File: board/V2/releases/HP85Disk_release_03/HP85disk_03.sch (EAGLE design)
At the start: 105 parts, among them J1 POWER_JACKSUPER_BOMB_DIGITY, J3 503398-1892, J4 USB_MINI-B_SMT, Q1 BSS138DW-7-F, U1 ATMEGA1284P-AUR, U10 MIC5205, U11 MAX811LEUS+T, U2 TPIC6A596DWRG4, U3 SN75ALS162DWR, U4 75ALS160, U6 SN74LVC1G32DCKR, U7 FT232RL, U8 TXS0104EDR, U9 LM1117, Y2 20MHz

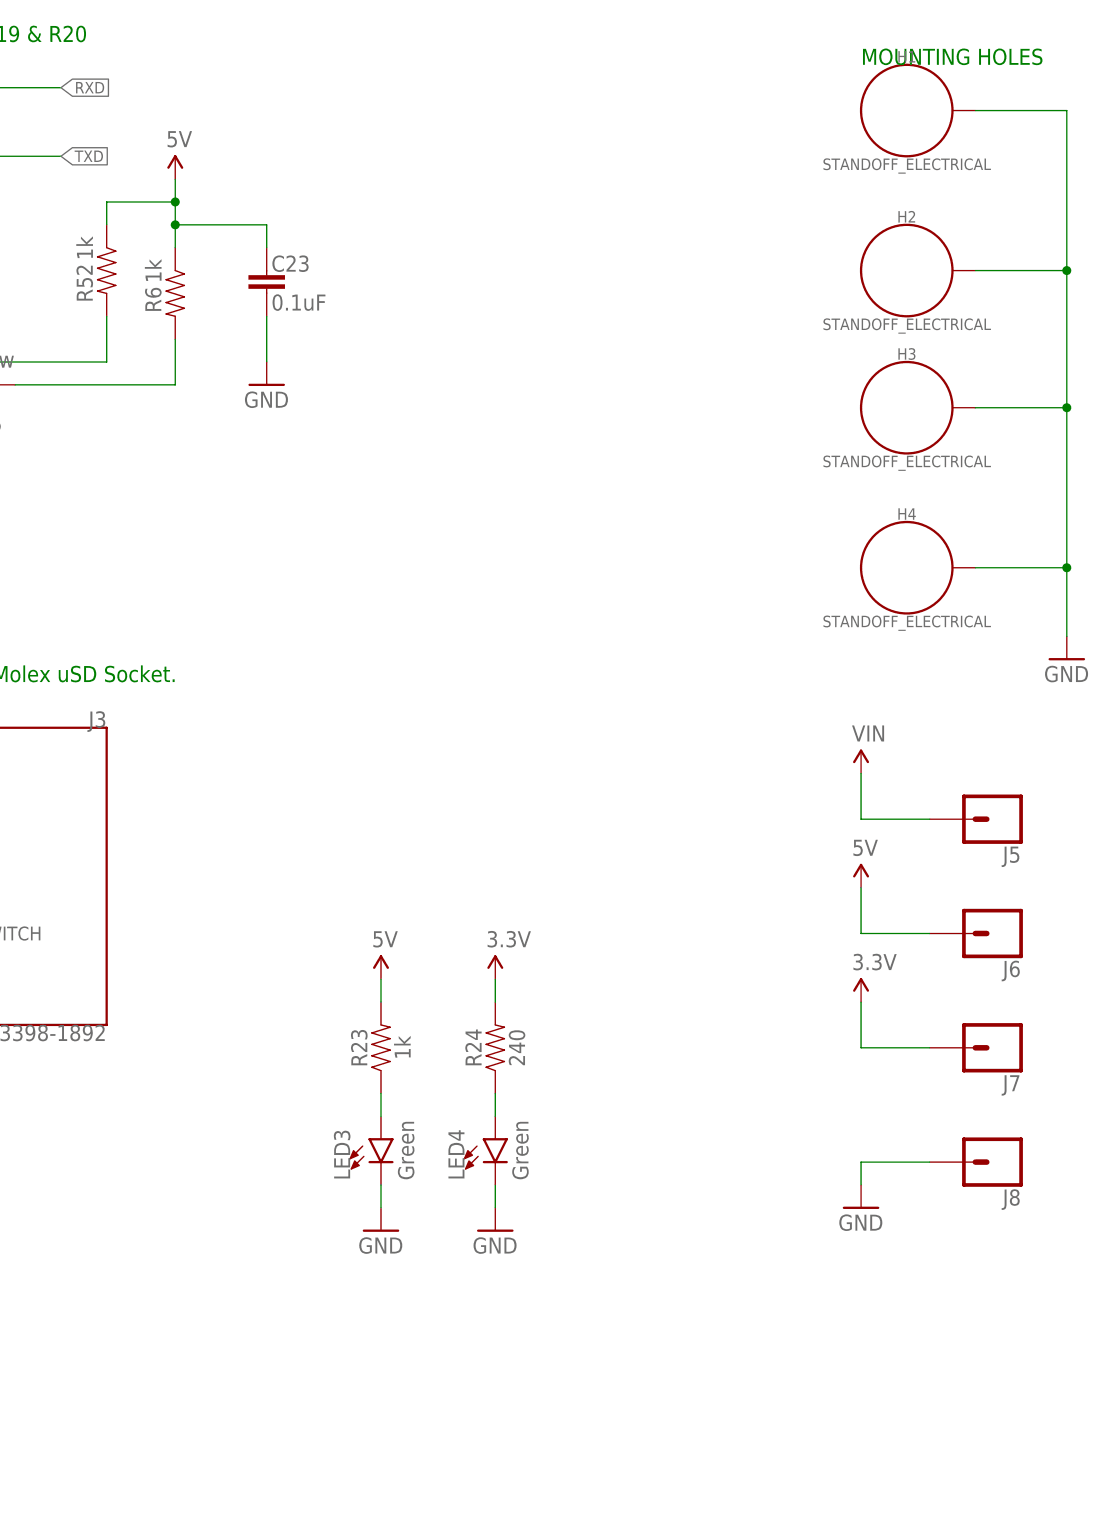
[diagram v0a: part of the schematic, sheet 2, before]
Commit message: Added RTC DS1703 - page 2 U5
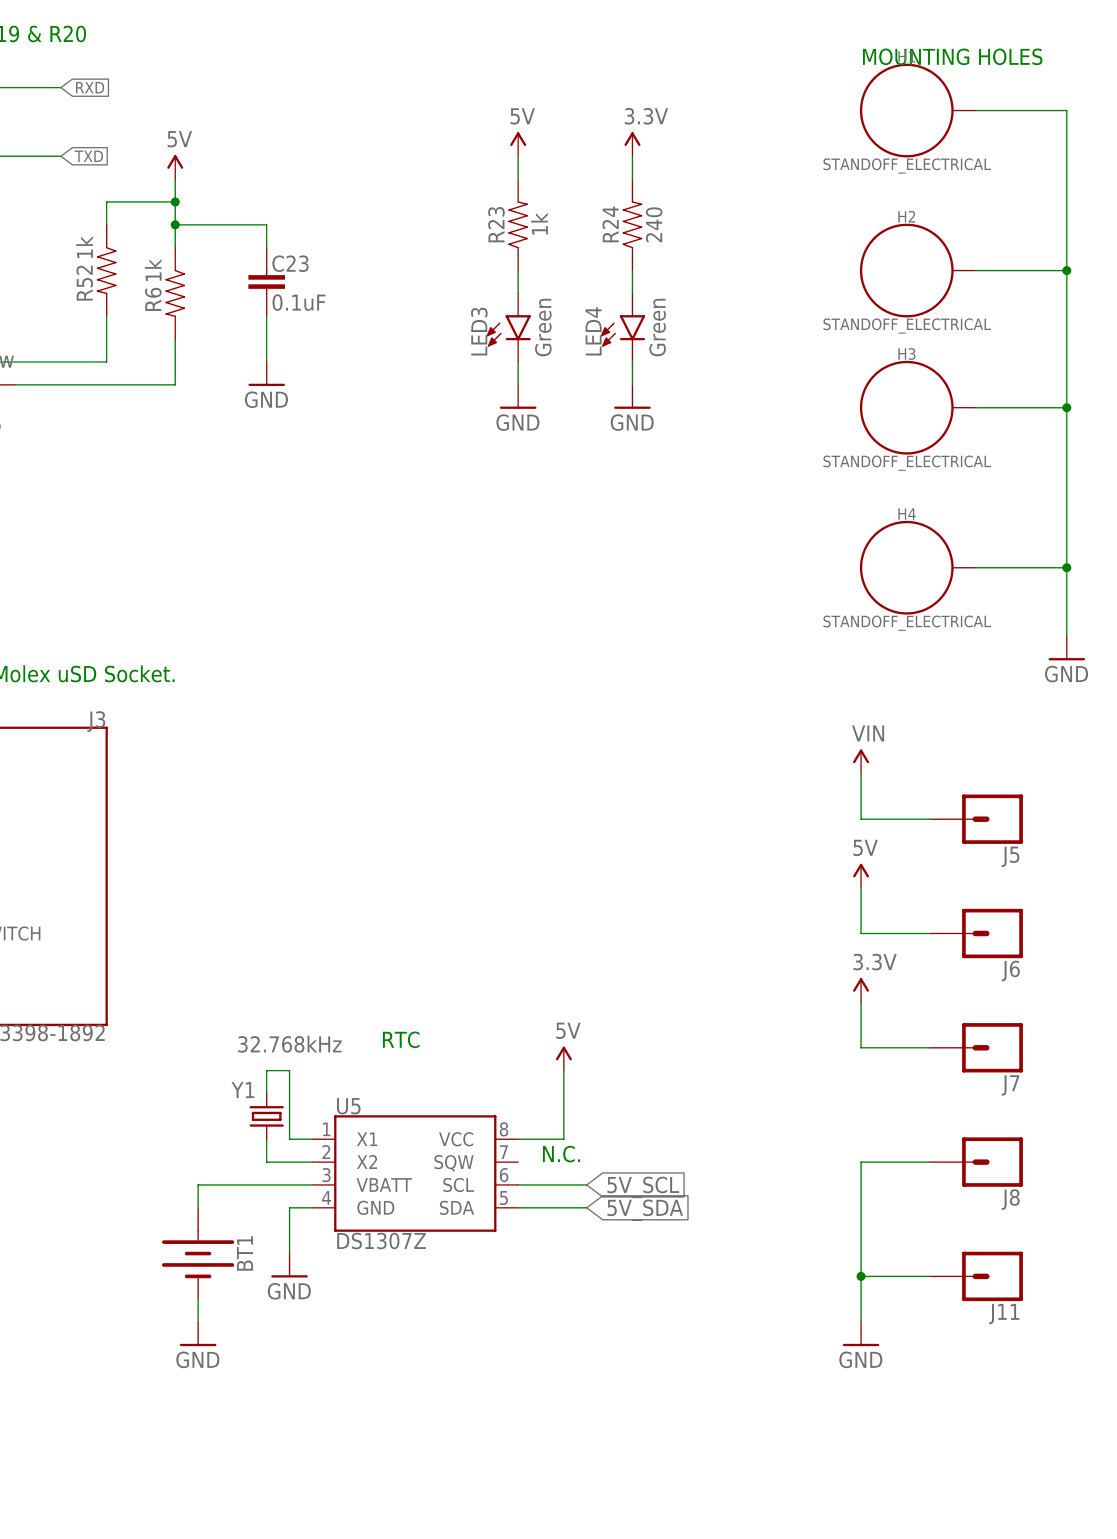
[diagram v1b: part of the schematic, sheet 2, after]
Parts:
- added BT1: (no value), SparkFun-Batteries:BATTERY-12MM_PTH
- added J11: (no value), SparkFun-Connectors:CONN_01
- added U5: DS1307Z, SparkFun-Clocks:DS1307Z
- added Y1: 32.768kHz, SparkFun-Clocks:CRYSTAL-32.768KHZSMD-2X6
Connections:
- new net N$16: U5.X1, Y1.2
- new net N$17: BT1.+, U5.VBATT
- new net N$18: U5.X2, Y1.1
- net 5V: now also U5.VCC
- net 5V_SCL: now also U5.SCL
- net 5V_SDA: now also U5.SDA
- net GND: now also BT1.-, J11.1, U5.GND
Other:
- note added: "N.C."
- note added: "RTC"
- moved on the sheet: LED3, LED4, R23, R24

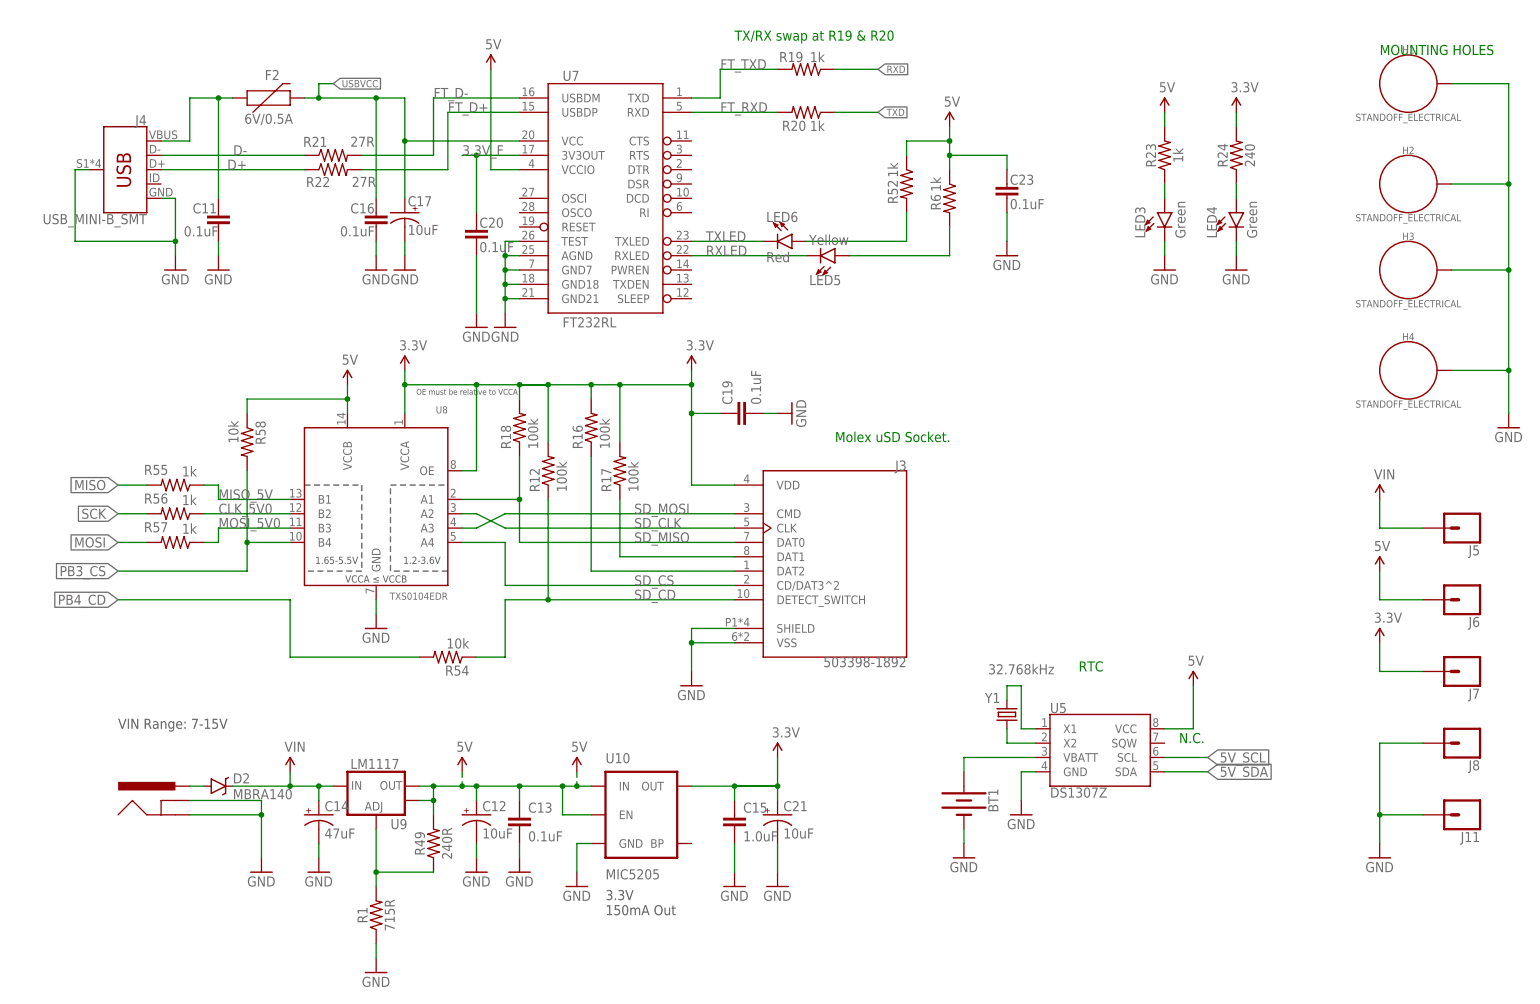
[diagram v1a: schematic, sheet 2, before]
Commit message: changed SDcard SPI bufffers to 74ACT125 and 74LVC125
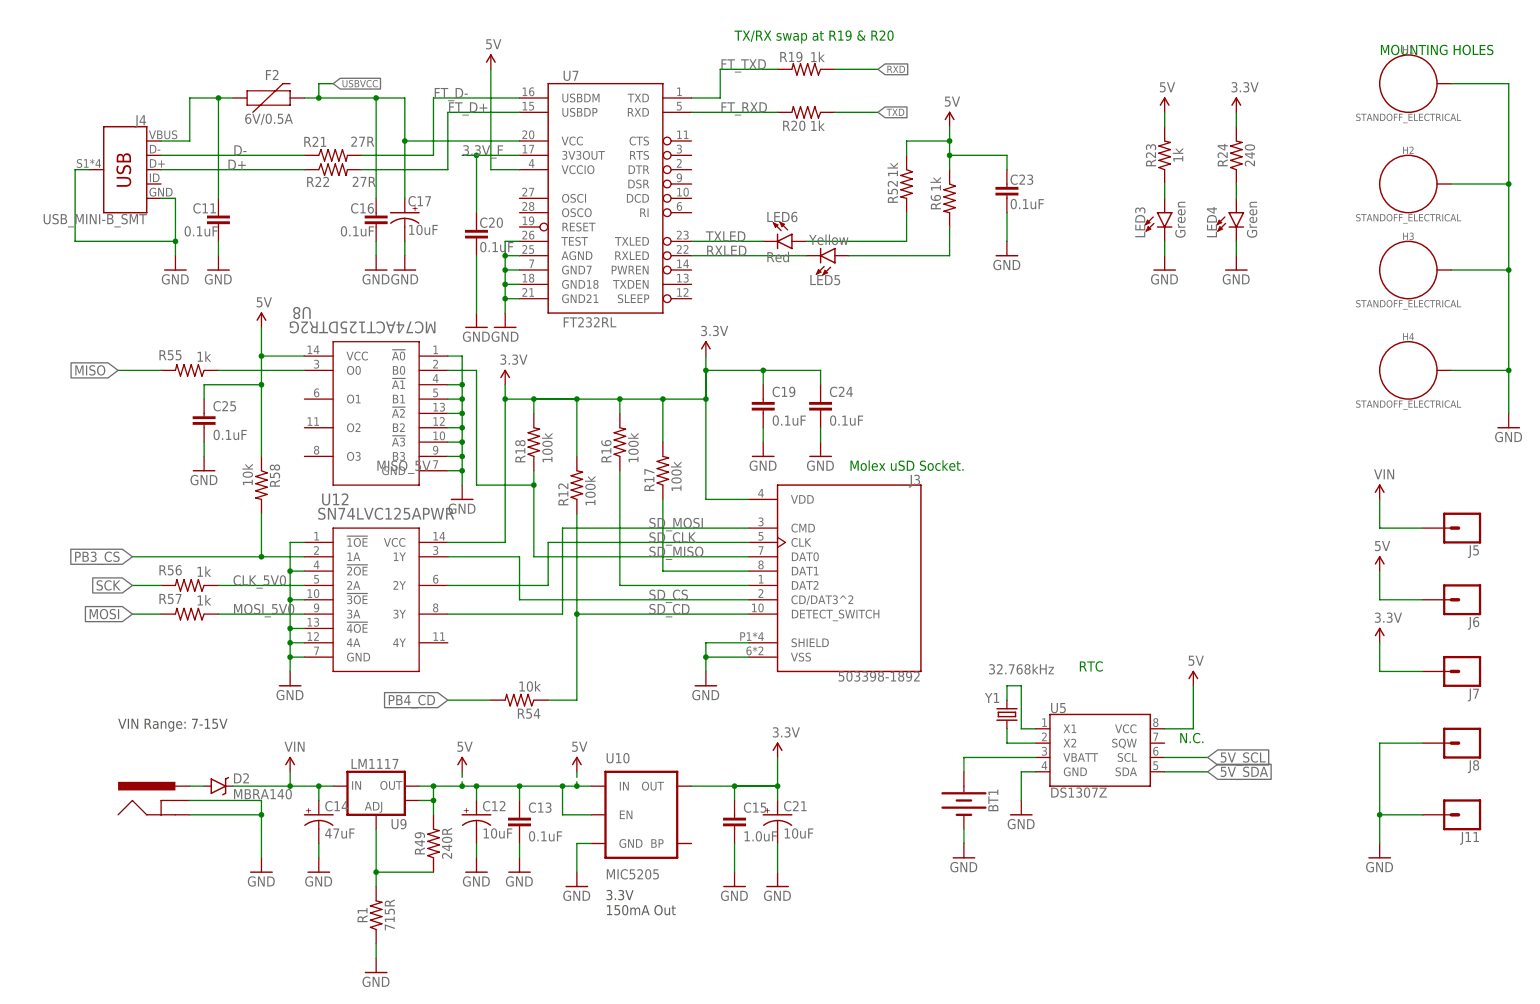
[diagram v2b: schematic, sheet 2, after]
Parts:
- added C24, C25: 0.1uF, SparkFun-Capacitors:0.1UF-0603-25V-(+80/-20%)
- added U12: SN74LVC125APWR, JaysOWL_Library:SN74LVC125APWR
- U8: value TXS0104EDR -> MC74ACT125DTR2G; device SparkFun-DigitalIC:TXB0104PWRSOIC14 -> JaysOWL_Library:MC74ACT125DTR2G
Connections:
- net 3.3V: now also C24.1, U12.VCC; no longer U8.OE, U8.VCCA
- net 5V: now also C25.1, U8.VCC; no longer U8.VCCB
- net CLK_5V0: now also U12.2A; no longer U8.B2
- net GND: now also C24.2, C25.2, U12.!1OE, U12.!2OE, U12.!3OE, U12.!4OE, U12.4A, U12.GND, U8.!A0, U8.!A1, U8.!A2, U8.!A3, U8.B1, U8.B2, U8.B3
- net MISO_5V: now also U8.O0; no longer U8.B1
- net MOSI_5V0: now also U12.3A; no longer U8.B3
- net PB3_CS: now also U12.1A; no longer U8.B4
- net SD_CLK: now also U12.2Y; no longer U8.A2
- net SD_CS: now also U12.1Y; no longer U8.A4
- net SD_MISO: now also U8.B0; no longer U8.A1
- net SD_MOSI: now also U12.3Y; no longer U8.A3
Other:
- note removed: "OE must be relative to VCCA"
- moved on the sheet: C19, J3, R12, R16, R17, R18, R54, R55, R56, R57, R58

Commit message: fixed SDCArd pullups. set ftdi series R to 120R. board cleaanup
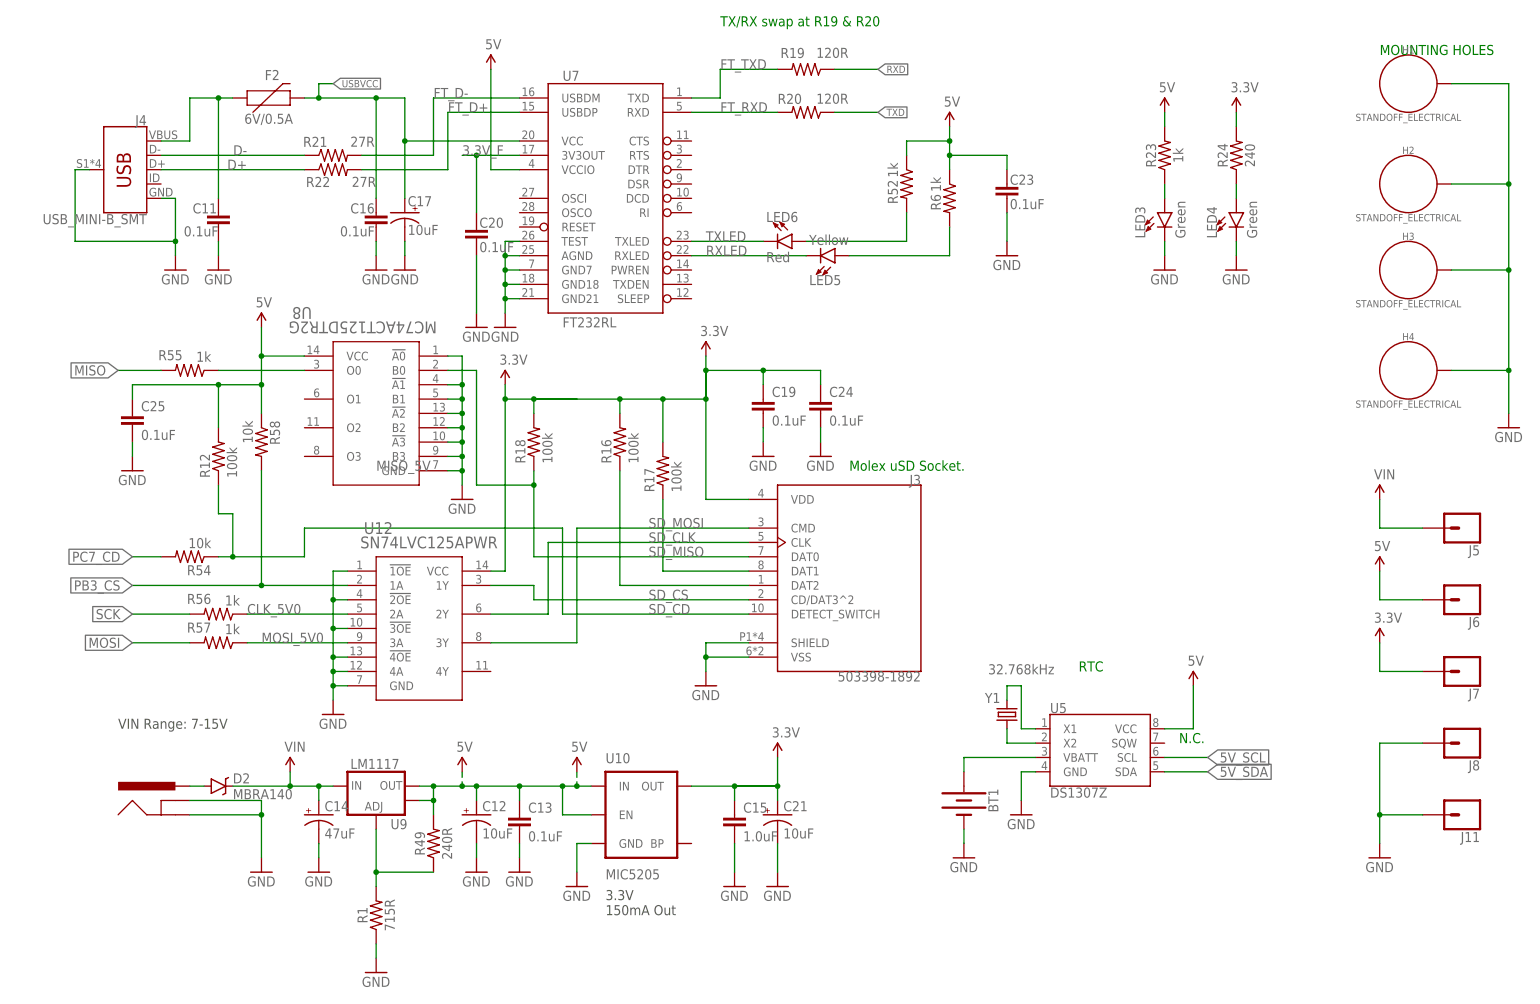
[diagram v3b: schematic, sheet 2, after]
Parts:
- removed R37: 10K, SparkFun-Resistors:10KOHM-0603-1/10W-1%
- R19, R20: value 1k -> 120R
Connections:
- removed net PB4_CD: R37.1, R54.2, U1.PB4(SS/OC0B)
- new net PC7_CD: R54.2, U1.PC7(TOSC2)
- net 3.3V: no longer R12.2
- net 5V: now also R12.2; no longer R37.2
- net N$10: now also U1.PB4(SS/OC0B); no longer U1.PC7(TOSC2)
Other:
- moved on the sheet: C25, LED1, LED2, R12, R2, R53, R54, R56, R57, R58, U12

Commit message: released versions of board files
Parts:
- R24: value 240 -> 240R
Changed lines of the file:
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@@
 <attribute name="PROD_ID" value="DIO-09910"/>
 </part>
-<part name="R24" library="SparkFun-Resistors" deviceset="4.7KOHM" device="-0603-1/10W-1%" value="240"/>
+<part name="R24" library="SparkFun-Resistors" deviceset="4.7KOHM" device="-0603-1/10W-1%" value="240R"/>
 <part name="GND25" library="SparkFun" deviceset="GND" device=""/>
 <part name="LED4" library="SparkFun-LED" deviceset="LED" device="1206" value="Green">
@@
 <pinref part="R30" gate="G$1" pin="2"/>
 <wire x1="200.66" y1="43.18" x2="205.74" y2="43.18" width="0.1524" layer="91"/>
-<wire x1="205.74" y1="43.18" x2="205.74" y2="37.084" width="0.1524" layer="91"/>
+<wire x1="205.74" y1="43.18" x2="205.74" y2="36.83" width="0.1524" layer="91"/>
 <wire x1="205.74" y1="36.83" x2="205.74" y2="27.94" width="0.1524" layer="91"/>
 <wire x1="205.74" y1="27.94" x2="220.98" y2="27.94" width="0.1524" layer="91"/>
@@
 <pinref part="R31" gate="G$1" pin="2"/>
 <wire x1="200.66" y1="36.83" x2="205.74" y2="36.83" width="0.1524" layer="91"/>
-<wire x1="205.74" y1="36.83" x2="205.74" y2="37.084" width="0.1524" layer="91"/>
-<junction x="205.74" y="37.084"/>
 <wire x1="246.38" y1="73.66" x2="254" y2="73.66" width="0.1524" layer="91"/>
 <junction x="246.38" y="73.66"/>
@@
 <pinref part="Q1" gate="A" pin="G1"/>
 <pinref part="Q1" gate="A" pin="G2"/>
-</segment>
-</net>
+<junction x="205.74" y="36.83"/>
+</segment>
+</net>

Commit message: updated pcb. rotated micro SD socket. updated gerbers
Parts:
- U10: value MIC5205 -> LP5907MFX-3.3
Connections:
- net N$3 renamed XT1
- net N$4 renamed XT2
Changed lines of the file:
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@@
 <part name="C14" library="SparkFun-Capacitors" deviceset="47UF-POLAR" device="-PANASONIC_D-35V-20%" value="47uF"/>
 <part name="GND21" library="SparkFun" deviceset="GND" device=""/>
-<part name="U10" library="SparkFun-PowerIC" deviceset="MIC5205" device="3.3V" value="MIC5205"/>
+<part name="U10" library="SparkFun-PowerIC" deviceset="MIC5205" device="3.3V" value="LP5907MFX-3.3"/>
 <part name="GND22" library="SparkFun" deviceset="GND" device=""/>
 <part name="C15" library="SparkFun-Capacitors" deviceset="1.0UF" device="-0603-16V-10%" value="1.0uF"/>
@@
 </segment>
 </net>
-<net name="N$3" class="0">
+<net name="XT1" class="0">
 <segment>
 <wire x1="58.42" y1="114.3" x2="40.894" y2="114.3" width="0.1524" layer="91"/>
@@
 <junction x="35.56" y="119.38"/>
 <pinref part="U1" gate="G$1" pin="XTAL1"/>
+<label x="45.72" y="114.3" size="1.778" layer="95"/>
 </segment>
 </net>
-<net name="N$4" class="0">
+<net name="XT2" class="0">
 <segment>
 <wire x1="58.42" y1="109.22" x2="35.56" y2="109.22" width="0.1524" layer="91"/>
@@
 <junction x="35.56" y="109.22"/>
 <pinref part="U1" gate="G$1" pin="XTAL2"/>
+<label x="45.72" y="109.22" size="1.778" layer="95"/>
 </segment>
 </net>
